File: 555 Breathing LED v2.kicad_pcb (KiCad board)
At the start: 2 copper layers, 12 parts, among them Q1 PN2222A, U1 LMC555xN

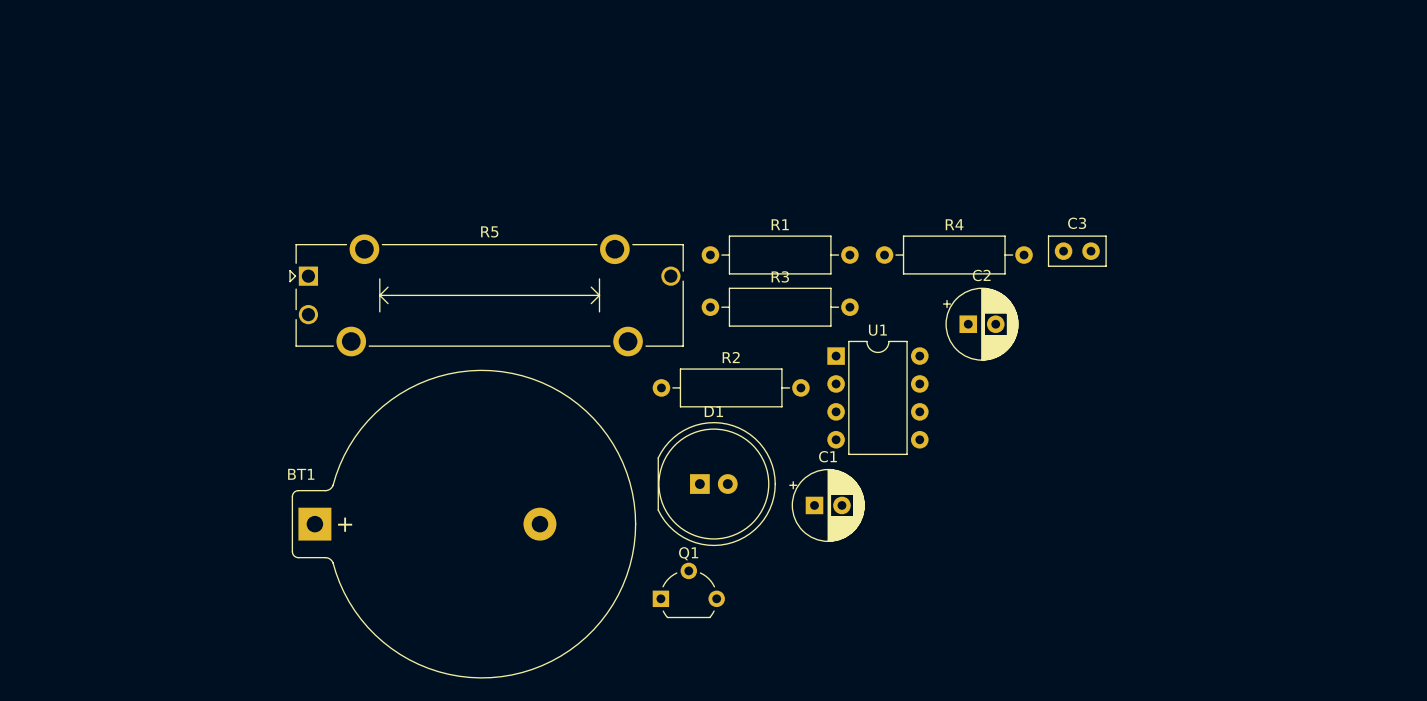
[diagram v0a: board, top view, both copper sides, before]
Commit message: moved pcb components
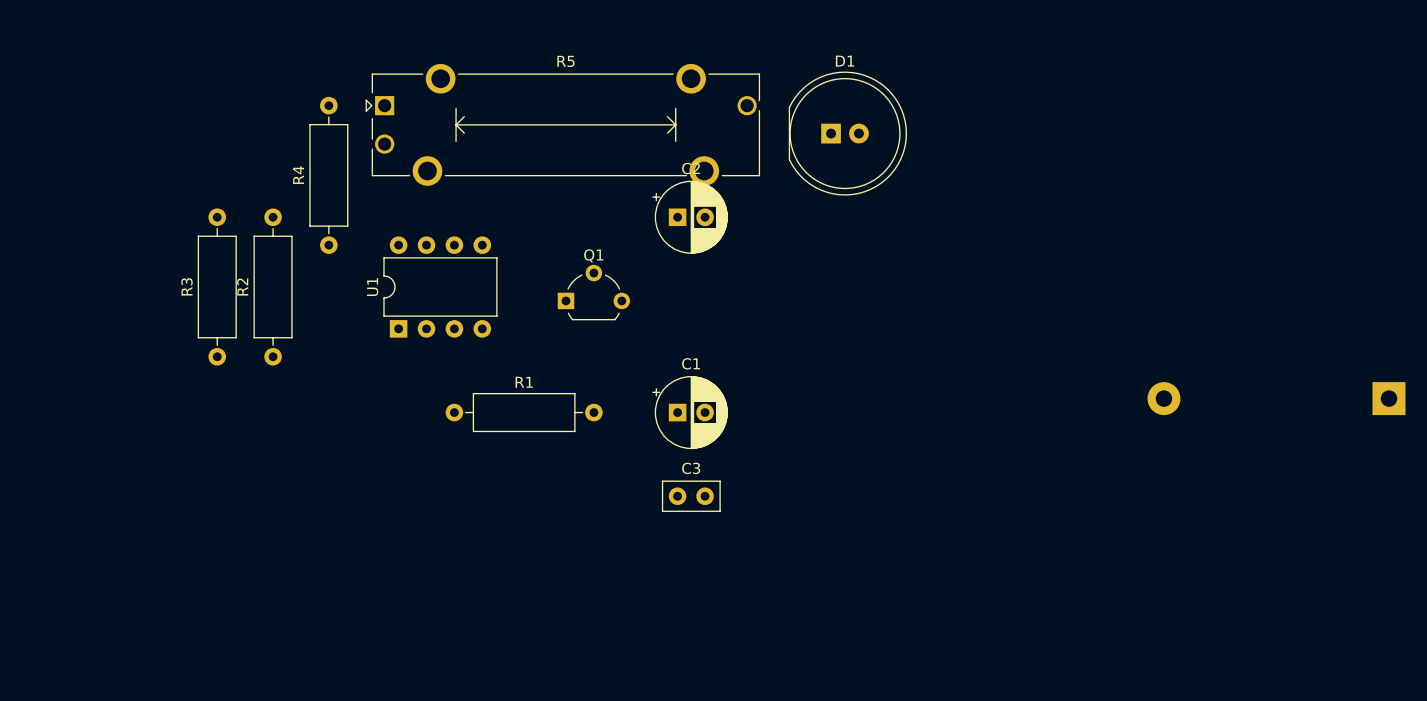
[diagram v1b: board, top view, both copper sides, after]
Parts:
- BT1: moved to B.Cu
- moved BT1 98.5 mm to (176.5, 99.1), turned to 180 degrees
- moved R4 50.6 mm to (80.0, 85.1), turned to 90 degrees
- moved R3 45.1 mm to (69.8, 95.2), turned to 90 degrees
- moved C3 41.6 mm to (111.8, 108.0)
- moved U1 39.9 mm to (86.4, 92.7), turned to 90 degrees
- moved R2 35.5 mm to (74.9, 95.2), turned to 90 degrees
- moved D1 34.1 mm to (125.7, 74.9)
- moved Q1 28.5 mm to (101.6, 90.2)
- moved C2 28.2 mm to (111.8, 82.5)
- moved R1 27.4 mm to (91.4, 100.3)
- moved R5 17.0 mm to (85.1, 72.4)
- moved C1 15.1 mm to (111.8, 100.3)

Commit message: developed pcb
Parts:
- added ?: LOGO, 555-Breathing-LED-v2:M5 Logo, F.Cu at (66.0, 91.4)
- added ?: LOGO, 555-Breathing-LED-v2:Smule Logo, F.Cu at (73.7, 93.2)
- moved BT1 52.7 mm to (125.7, 85.1), turned to 170 degrees
- moved C3 37.0 mm to (80.0, 88.9), turned to 180 degrees
- moved R4 18.1 mm to (68.6, 71.1), turned to 0 degrees
- moved C1 17.8 mm to (110.5, 82.5), turned to 270 degrees
- moved R3 17.8 mm to (68.6, 77.5), turned to 0 degrees
- moved Q1 17.7 mm to (118.1, 83.8), turned to 270 degrees
- moved R2 13.1 mm to (68.6, 83.8), turned to 0 degrees
- moved R1 12.7 mm to (99.1, 90.2)
- moved C2 11.4 mm to (100.3, 82.5), turned to 270 degrees
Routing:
- net VCC: track 0.00 -> 95.7 mm
- net Net-(D1-Pad1): track 0.00 -> 76.7 mm
- net Net-(C2-Pad1): track 0.00 -> 35.8 mm
- net Net-(R3-Pad2): track 0.00 -> 26.1 mm
- net Net-(C1-Pad1): track 0.00 -> 24.0 mm
- net Net-(C3-Pad1): track 0.00 -> 15.5 mm
- net Net-(D1-Pad2): track 0.00 -> 14.6 mm
- net out: track 0.00 -> 8.67 mm
- net Net-(R4-Pad2): track 0.00 -> 4.34 mm
- net (no net): vias 0 -> 2
- added copper zone on F.Cu, net GND
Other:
- board outline added: 74.9 x 31.8 mm
- board text added: "Fall 2021"
- board text added: "M5 Soldering Workshop I 2021"
- board text added: "PCB Designed by Zachary Welch 2024"
- board text added: "Saturday is Makerday!"

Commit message: Finished PCB
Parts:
- added REF**: MountingHole_3.2mm_M3, MountingHole:MountingHole_3.2mm_M3, F.Cu at (64.8, 69.8)
- added REF**: MountingHole_3.2mm_M3, MountingHole:MountingHole_3.2mm_M3, F.Cu at (130.8, 97.8)
- added SW1: SW_SPDT, 555-Breathing-LED-v2:MHS12204_SPDT, F.Cu at (61.0, 81.3)
- BT1: footprint Battery:BatteryHolder_Keystone_107_1x23mm -> 555-Breathing-LED-v2:BatteryHolder_MPD_BA9VPC_1xPP3noholes
- moved D1 9.67 mm to (129.5, 83.8), turned to 180 degrees
- moved BT1 8.52 mm to (121.9, 77.5), turned to 180 degrees
- moved ? 7.41 mm to (59.7, 95.2)
- moved ? 6.23 mm to (68.6, 96.8)
- moved Q1 2.54 mm to (118.1, 81.3)
- moved R2 2.54 mm to (66.0, 83.8)
- moved R3 2.54 mm to (66.0, 77.5)
- moved R4 2.54 mm to (66.0, 71.1)
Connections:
- BT1 pad 1: VCC -> Net-(BT1-Pad1)
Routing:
- net Net-(BT1-Pad1): track 0.00 -> 81.1 mm
- net Net-(C1-Pad1): track 24.0 -> 18.2 mm
- net Net-(D1-Pad2): track 14.6 -> 9.94 mm
- net VCC: track 95.7 -> 91.5 mm
- net Net-(R4-Pad2): track 4.34 -> 6.88 mm
- net Net-(R3-Pad2): track 26.1 -> 28.6 mm
- net Net-(D1-Pad1): track 76.7 -> 77.3 mm
- net (no net): vias 2 -> 0
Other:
- board size 74.9 x 31.8 mm -> 80.8 x 35.6 mm
